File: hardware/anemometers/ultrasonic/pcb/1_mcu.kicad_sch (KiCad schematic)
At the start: 59 parts, among them Q1 SI2301CDS-T1-GE3, SW1 B3U-1000P, U1 TCAN330GDCNR, U12 Sort_Symbol, U14 Sort_Symbol, U15 Sort_Symbol, U16 Sort_Symbol, U2 STM32L476RGT6, U3 XC6206P332MR, X1 32.768KHz, X2 25M

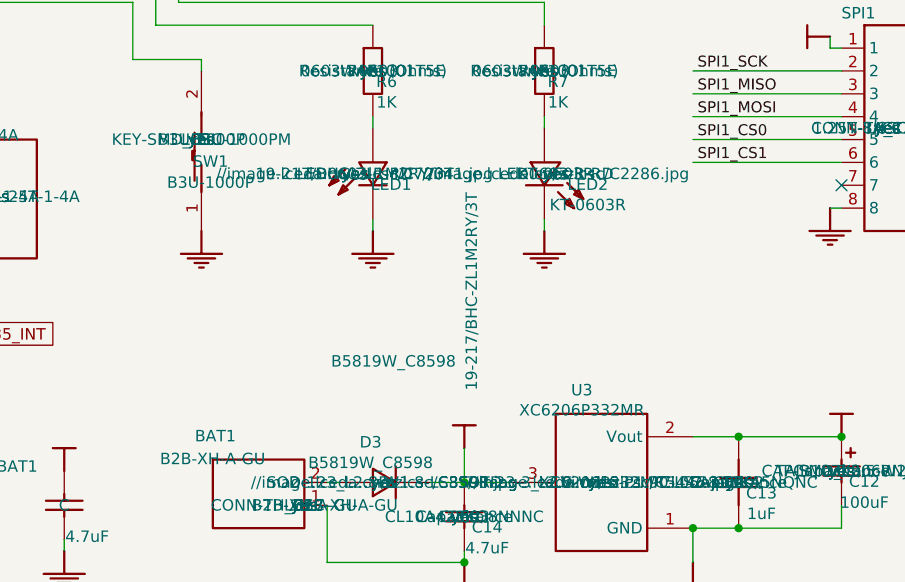
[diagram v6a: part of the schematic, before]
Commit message: Fix LED
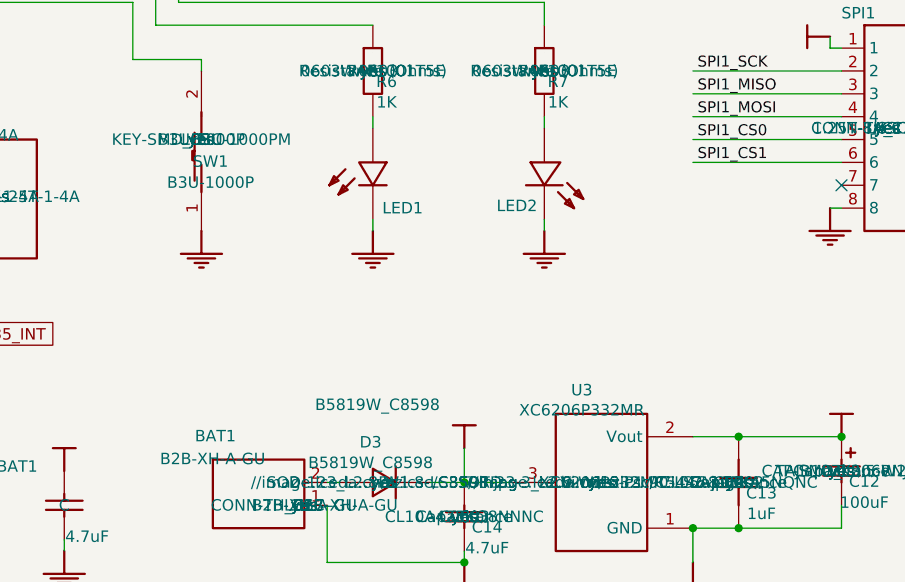
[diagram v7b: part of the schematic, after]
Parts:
- LED1: value 19-217/BHC-ZL1M2RY/3T -> XL-1608UBC-06A; Manufacturer EVERLIGHT -> XINGLIGHT; Manufacturer Part 19-217/BHC-ZL1M2RY/3T -> XL-1608UBC-06A; Supplier Part C72041 -> C7371904
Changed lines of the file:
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@@
 		(dnp no)
 		(property "Reference" "LED2"
-			(at 293.116 152.3238 90)
+			(at 285.242 154.686 90)
 			(effects
 				(font
@@
 		)
 		(property "Value" "KT-0603R"
-			(at 293.116 154.5844 90)
+			(at 299.212 156.718 90)
 			(effects
 				(font
 					(size 1.27 1.27)
 				)
+				(hide yes)
 			)
 		)
@@
 					(size 1.27 1.27)
 				)
+				(hide yes)
 			)
 		)
@@
 					(size 1.27 1.27)
 				)
+				(hide yes)
 			)
 		)
@@
 					(size 1.27 1.27)
 				)
+				(hide yes)
 			)
 		)
@@
 					(size 1.27 1.27)
 				)
+				(hide yes)
 			)
 		)
@@
 					(size 1.27 1.27)
 				)
+				(hide yes)
 			)
 		)
@@
 					(size 1.27 1.27)
 				)
+				(hide yes)
 			)
 		)
@@
 		)
 		(property "spiceSymbolName" "B5819W_C8598"
-			(at 271.526 171.958 0)
+			(at 269.748 176.784 0)
 			(effects
 				(font
@@
 		(dnp no)
 		(property "Reference" "LED1"
-			(at 271.272 152.3238 90)
+			(at 272.542 154.94 90)
 			(effects
 				(font
@@
 			)
 		)
-		(property "Value" "19-217/BHC-ZL1M2RY/3T"
+		(property "Value" "XL-1608UBC-06A"
 			(at 280.2128 164.1856 0)
 			(effects
@@
 					(size 1.27 1.27)
 				)
+				(hide yes)
 			)
 		)
@@
 			)
 		)
-		(property "Manufacturer Part" "19-217/BHC-ZL1M2RY/3T"
+		(property "Manufacturer Part" "XL-1608UBC-06A"
 			(at 267.208 151.13 0)
 			(effects
@@
 			)
 		)
-		(property "Manufacturer" "EVERLIGHT"
+		(property "Manufacturer" "XINGLIGHT"
 			(at 267.208 151.13 0)
 			(effects
@@
 			)
 		)
-		(property "Supplier Part" "C72041"
+		(property "Supplier Part" "C7371904"
 			(at 267.208 151.13 0)
 			(effects
@@
 					(size 1.27 1.27)
 				)
+				(hide yes)
 			)
 		)
@@
 					(size 1.27 1.27)
 				)
+				(hide yes)
 			)
 		)
@@
 					(size 1.27 1.27)
 				)
+				(hide yes)
 			)
 		)
@@
 					(size 1.27 1.27)
 				)
+				(hide yes)
 			)
 		)
@@
 					(size 1.27 1.27)
 				)
+				(hide yes)
 			)
 		)
@@
 					(size 1.27 1.27)
 				)
+				(hide yes)
 			)
 		)

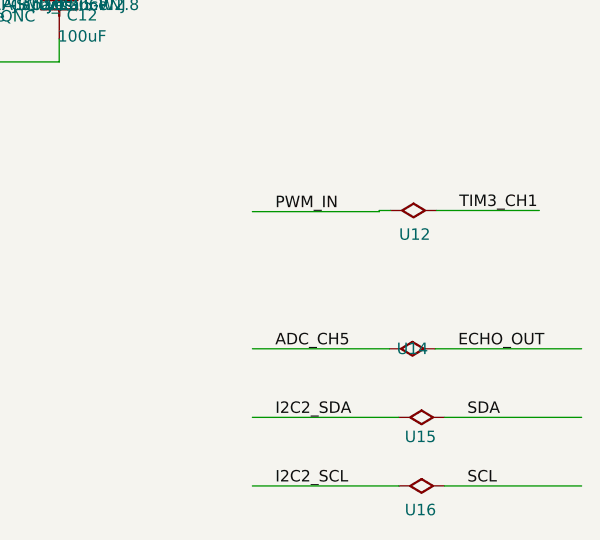
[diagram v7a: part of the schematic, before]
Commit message: Update to BMI270
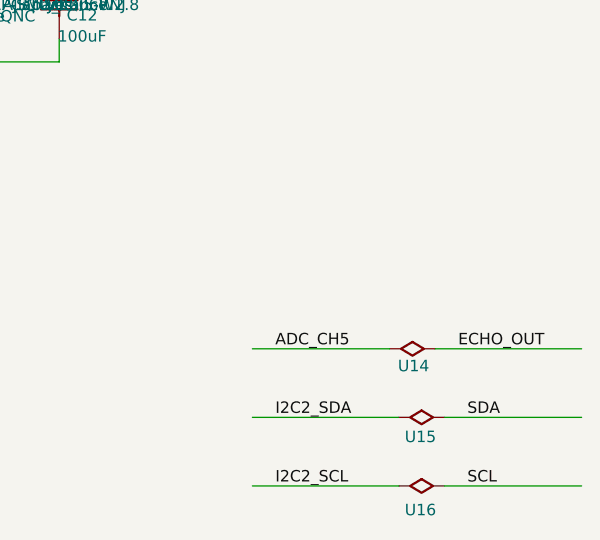
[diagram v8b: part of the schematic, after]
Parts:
- removed U12: Sort_Symbol, ProDoc_Qin-easyedapro:, symbol ProDoc_Qin-easyedapro:d8f82a34bc8fbed0
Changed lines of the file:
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@@
 	(wire
 		(pts
-			(xy 356.87 207.01) (xy 356.87 207.137)
-		)
-		(stroke
-			(width 0)
-			(type default)
-		)
-	)
-	(wire
-		(pts
 			(xy 321.31 180.34) (xy 309.88 180.34)
 		)
@@
 	(wire
 		(pts
-			(xy 363.22 207.01) (xy 374.65 207.01)
-		)
-		(stroke
-			(width 0)
-			(type default)
-		)
-	)
-	(wire
-		(pts
 			(xy 107.95 63.5) (xy 92.71 63.5)
 		)
@@
 	(wire
 		(pts
-			(xy 356.87 207.01) (xy 358.14 207.01)
-		)
-		(stroke
-			(width 0)
-			(type default)
-		)
-	)
-	(wire
-		(pts
 			(xy 293.37 93.98) (xy 293.37 104.14)
 		)
@@
 	(wire
 		(pts
-			(xy 356.87 207.137) (xy 342.773 207.137)
-		)
-		(stroke
-			(width 0)
-			(type default)
-		)
-	)
-	(wire
-		(pts
 			(xy 321.31 190.5) (xy 309.88 190.5)
 		)
@@
 		)
 	)
-	(label "PWM_IN"
-		(at 345.313 207.137 0)
-		(effects
-			(font
-				(size 1.27 1.27)
-			)
-			(justify left bottom)
-		)
-	)
 	(label "USART2_TX"
 		(at 83.058 199.39 0)
@@
 		)
 	)
-	(label "TIM3_CH1"
-		(at 365.76 207.01 0)
-		(effects
-			(font
-				(size 1.27 1.27)
-			)
-			(justify left bottom)
-		)
-	)
 	(label "SPI1_MISO"
 		(at 161.29 74.93 90)
@@
 	)
 	(symbol
-		(lib_name "d8f82a34bc8fbed0_4")
-		(lib_id "ProDoc_Qin-easyedapro:d8f82a34bc8fbed0")
-		(at 360.68 207.01 0)
-		(unit 1)
-		(exclude_from_sim no)
-		(in_bom no)
-		(on_board yes)
-		(dnp no)
-		(property "Reference" "U12"
-			(at 360.807 209.677 0)
-			(effects
-				(font
-					(size 1.27 1.27)
-				)
-			)
-		)
-		(property "Value" "Sort_Symbol"
-			(at 361.315 202.311 0)
-			(effects
-				(font
-					(size 1.27 1.27)
-				)
-				(hide yes)
-			)
-		)
-		(property "Footprint" "ProDoc_Qin-easyedapro:"
-			(at 360.68 207.01 0)
-			(effects
-				(font
-					(size 1.27 1.27)
-				)
-				(hide yes)
-			)
-		)
-		(property "Datasheet" ""
-			(at 360.68 207.01 0)
-			(effects
-				(font
-					(size 1.27 1.27)
-				)
-				(hide yes)
-			)
-		)
-		(property "Description" ""
-			(at 360.68 207.01 0)
-			(effects
-				(font
-					(size 1.27 1.27)
-				)
-				(hide yes)
-			)
-		)
-		(pin ""
-		)
-		(pin ""
-		)
-		(instances
-			(project ""
-				(path "/4adc9a43-9f3a-44e1-ab61-563de3288fd4/cbb659ca-1b7c-4a31-89d0-9b7906cdfb95"
-					(reference "U?")
-					(unit 1)
-				)
-			)
-			(project ""
-				(path "/a30633bf-68dd-4888-88d6-d1ee9beba30f/d8b5ed7a-2a3a-4cba-9ce3-8a59c7975a1d"
-					(reference "U12")
-					(unit 1)
-				)
-			)
-		)
-	)
-	(symbol
 		(lib_id "ProDoc_Qin-easyedapro:3.3V")
 		(at 142.24 167.64 180)
@@
 		(dnp no)
 		(property "Reference" "U14"
-			(at 360.553 222.377 0)
+			(at 360.68 224.282 0)
 			(effects
 				(font
